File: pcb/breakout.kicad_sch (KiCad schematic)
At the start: 1 part, among them J14 PINHD_1x8_Female

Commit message: Add files via upload
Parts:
- removed J14: PINHD_1x8_Female, Connector_PinSocket_2.54mm:PinSocket_1x08_P2.54mm_Vertical, symbol PCM_SL_Pin_Headers:PINHD_1x8_Female
- added J10, J12: PINHD_1x4_Female, Connector_PinSocket_2.54mm:PinSocket_1x04_P2.54mm_Vertical, symbol PCM_SL_Pin_Headers:PINHD_1x4_Female
- added J13, J14: PINHD_1x5_Male, Connector_PinHeader_1.00mm:PinHeader_1x05_P1.00mm_Vertical, symbol PCM_SL_Pin_Headers:PINHD_1x5_Male
- added J16: PINHD_1x2_Male, Connector_PinHeader_2.54mm:PinHeader_1x02_P2.54mm_Vertical, symbol PCM_SL_Pin_Headers:PINHD_1x2_Male
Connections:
- net +3.3V: now also J10.1, J16.1
- net GND: now also J10.2, J12.2, J16.2
- net SCL: now also J13.2
- net SDA: now also J13.1
- net SHDN1: now also J13.3
- net SHDN2: now also J13.4
- net SHDN3: now also J13.5
- new net NRST: J12.4, J14.5
- new net SWCLK: J12.1, J14.3
- new net SWDIO: J12.3, J14.4
- new net USART_RX: J10.3, J14.1
- new net USART_TX: J10.4, J14.2
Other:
- sheet TOF FrontLeft renamed TOF Front
- removed sheet TOF FrontRight

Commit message: Add files via upload
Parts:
- renumbered J13 to J15, J10 to J?, J12 to J?
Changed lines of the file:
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@@
   (symbol (lib_id "PCM_SL_Pin_Headers:PINHD_1x4_Female") (at 153.67 111.76 0) (unit 1)
     (in_bom yes) (on_board yes) (dnp no) (fields_autoplaced)
-    (property "Reference" "J10" (at 156.21 110.49 0)
+    (property "Reference" "J?" (at 156.21 110.49 0)
       (effects (font (size 1.27 1.27)) (justify left))
     )
@@
       (project "micromouse"
         (path "/77cbf270-6b61-4f1a-b1cd-1a823bc4a9d0"
-          (reference "J10") (unit 1)
+          (reference "J?") (unit 1)
         )
         (path "/77cbf270-6b61-4f1a-b1cd-1a823bc4a9d0/2b401192-29f1-4489-afec-f456074fa36a"
-          (reference "J10") (unit 1)
+          (reference "J5") (unit 1)
         )
       )
@@
   (symbol (lib_id "PCM_SL_Pin_Headers:PINHD_1x4_Female") (at 153.67 124.46 0) (unit 1)
     (in_bom yes) (on_board yes) (dnp no) (fields_autoplaced)
-    (property "Reference" "J12" (at 156.21 123.19 0)
+    (property "Reference" "J?" (at 156.21 123.19 0)
       (effects (font (size 1.27 1.27)) (justify left))
     )
@@
       (project "micromouse"
         (path "/77cbf270-6b61-4f1a-b1cd-1a823bc4a9d0"
-          (reference "J12") (unit 1)
+          (reference "J?") (unit 1)
         )
         (path "/77cbf270-6b61-4f1a-b1cd-1a823bc4a9d0/2b401192-29f1-4489-afec-f456074fa36a"
-          (reference "J19") (unit 1)
+          (reference "J3") (unit 1)
         )
       )
@@
   (symbol (lib_id "PCM_SL_Pin_Headers:PINHD_1x5_Male") (at 115.57 80.01 0) (mirror y) (unit 1)
     (in_bom yes) (on_board yes) (dnp no)
-    (property "Reference" "J13" (at 113.03 78.74 0)
+    (property "Reference" "J15" (at 113.03 78.74 0)
       (effects (font (size 1.27 1.27)) (justify left))
     )
@@
       (project "micromouse"
         (path "/77cbf270-6b61-4f1a-b1cd-1a823bc4a9d0/2b401192-29f1-4489-afec-f456074fa36a"
-          (reference "J13") (unit 1)
+          (reference "J15") (unit 1)
         )
       )
@@
   (symbol (lib_id "power:GND") (at 144.78 133.35 0) (unit 1)
     (in_bom yes) (on_board yes) (dnp no)
-    (property "Reference" "#PWR011" (at 144.78 139.7 0)
+    (property "Reference" "#PWR?" (at 144.78 139.7 0)
       (effects (font (size 1.27 1.27)) hide)
     )
@@
       (project "micromouse"
         (path "/77cbf270-6b61-4f1a-b1cd-1a823bc4a9d0"
-          (reference "#PWR011") (unit 1)
+          (reference "#PWR?") (unit 1)
         )
         (path "/77cbf270-6b61-4f1a-b1cd-1a823bc4a9d0/2b401192-29f1-4489-afec-f456074fa36a"
-          (reference "#PWR037") (unit 1)
+          (reference "#PWR048") (unit 1)
         )
       )

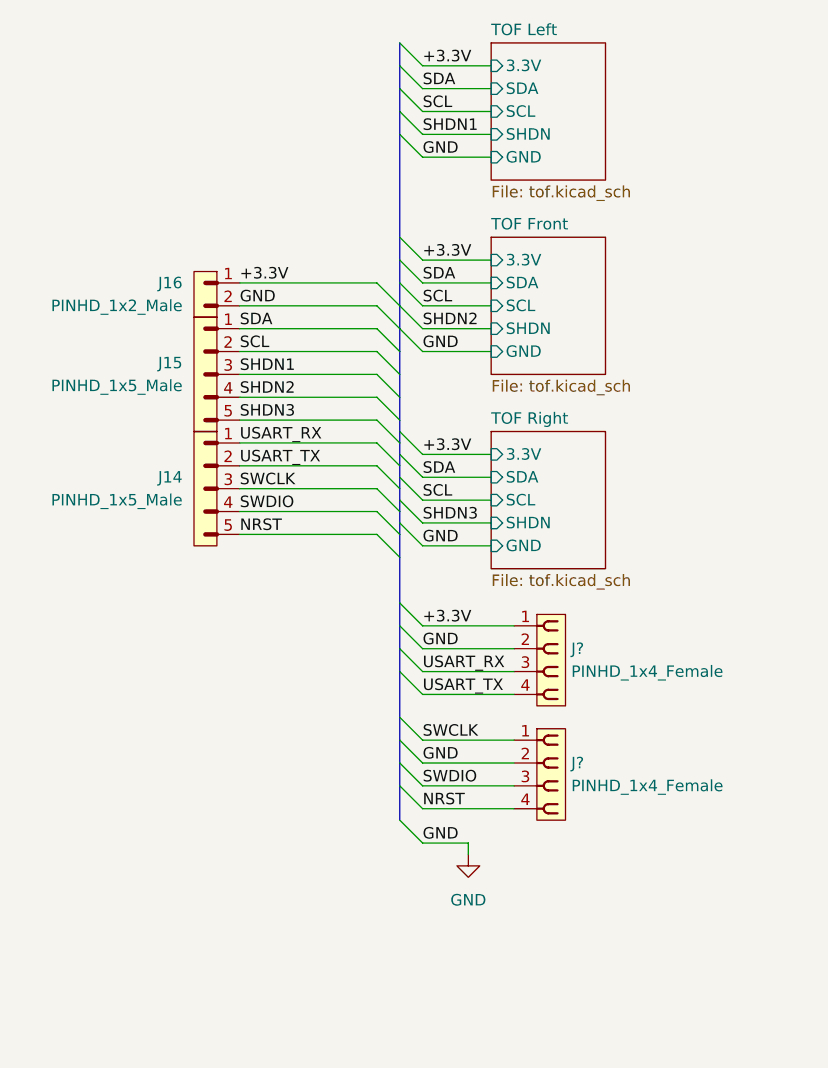
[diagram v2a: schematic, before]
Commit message: Fixed folder structure
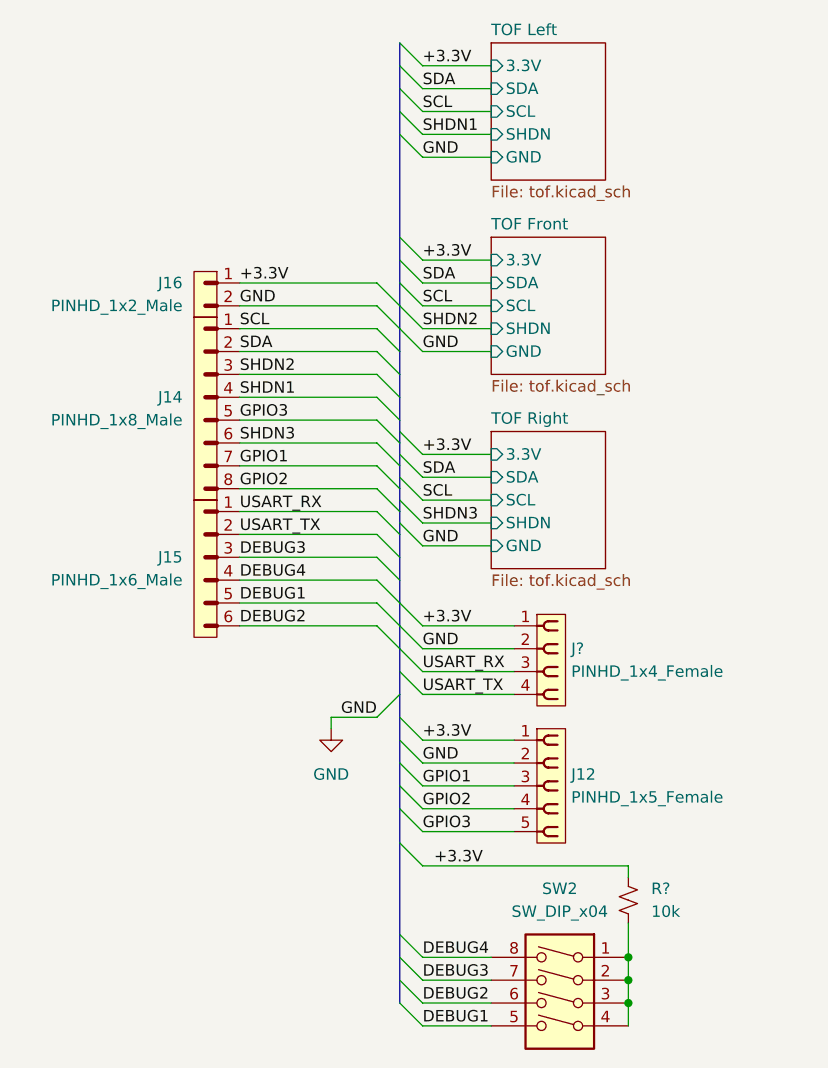
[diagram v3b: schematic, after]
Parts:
- removed J14, J15: PINHD_1x5_Male, Connector_PinHeader_1.00mm:PinHeader_1x05_P1.00mm_Vertical, symbol PCM_SL_Pin_Headers:PINHD_1x5_Male
- removed J?: PINHD_1x4_Female, Connector_PinSocket_2.54mm:PinSocket_1x04_P2.54mm_Vertical, symbol PCM_SL_Pin_Headers:PINHD_1x4_Female
- added J12: PINHD_1x5_Female, Connector_PinSocket_2.54mm:PinSocket_1x05_P2.54mm_Vertical, symbol PCM_SL_Pin_Headers:PINHD_1x5_Female
- added J14: PINHD_1x8_Male, Connector_PinHeader_2.54mm:PinHeader_2x04_P2.54mm_Vertical, symbol PCM_SL_Pin_Headers:PINHD_1x8_Male
- added J15: PINHD_1x6_Male, Connector_PinHeader_2.54mm:PinHeader_2x03_P2.54mm_Vertical, symbol PCM_SL_Pin_Headers:PINHD_1x6_Male
- added R?: 10k, Resistor_SMD:R_0603_1608Metric, symbol Device:R_Small_US
- added SW2: SW_DIP_x04, 218-4LPST:218-4LPST, symbol Switch:SW_DIP_x04
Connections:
- net +3.3V: now also J12.1, R?.1
- net GND: now also J12.2
- net SCL: now also J14.1
- net SDA: now also J14.2
- net SHDN1: now also J14.4
- net SHDN2: now also J14.3
- net SHDN3: now also J14.6
- net USART_RX: now also J15.1
- net USART_TX: now also J15.2
- new net: R?.2, SW2.1, SW2.2, SW2.3, SW2.4
- new net DEBUG1: J15.5, SW2.5
- new net DEBUG2: J15.6, SW2.6
- new net DEBUG3: J15.3, SW2.7
- new net DEBUG4: J15.4, SW2.8
- new net GPIO1: J12.3, J14.7
- new net GPIO2: J12.4, J14.8
- new net GPIO3: J12.5, J14.5
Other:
- company: (none) -> UCLA Micromouse 2023-24 Team 2
- title: (none) -> Mouse Potato
